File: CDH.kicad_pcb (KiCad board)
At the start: 2 copper layers, 45 parts, among them J3 G125-MH12605M4P, J4 Conn_ARM_JTAG_SWD_10, U1 STM32H745BITx, U2 MCP2562FDT-H_SN

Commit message: routing almost done
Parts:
- moved JP2 77.5 mm to (89.0, 37.0), turned to -90 degrees
- moved C27 73.1 mm to (77.0, 37.5)
- moved U2 72.1 mm to (81.8, 37.4)
- moved R6 69.8 mm to (88.5, 40.5), turned to -90 degrees
- moved C26 66.5 mm to (82.0, 41.0), turned to 0 degrees
- moved J4 62.8 mm to (29.0, 39.5), turned to 180 degrees
- moved PC104_H1 59.0 mm to (86.0, 55.0)
- moved J3 57.0 mm to (24.3, 55.4), turned to -90 degrees
- moved PC104_H2 52.2 mm to (90.0, 55.0)
- moved R8 51.4 mm to (40.8, 42.0), turned to 0 degrees
- moved C25 20.0 mm to (41.0, 76.0)
- moved SW_Reset1 17.6 mm to (41.0, 72.5)
- moved C24 14.5 mm to (34.5, 53.0)
- moved C28 10.8 mm to (82.9, 52.7), turned to 90 degrees
- moved R1 10.1 mm to (68.9, 37.7)
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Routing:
- net VDD: track 0.00 -> 74.9 mm
- net GND: track 0.00 -> 69.5 mm, vias 0 -> 2
- net /CS3: track 0.00 -> 52.7 mm
- net /CS2: track 0.00 -> 51.5 mm, vias 0 -> 1
- net Net-(JP1-B): track 0.00 -> 51.0 mm
- net /I2C2_SDA: track 0.00 -> 50.4 mm, vias 0 -> 1
- net /CS1: track 0.00 -> 50.3 mm
- net /I2C2_SCL: track 0.00 -> 49.7 mm, vias 0 -> 1
- net /FDCAN1_RX: track 0.00 -> 38.3 mm
- net /CANH_PC104: track 0.00 -> 29.2 mm
- net /CANL_PC104: track 0.00 -> 21.3 mm
- net /FDCAN1_TX: track 0.00 -> 15.1 mm
- net Net-(C23-Pad2): track 0.00 -> 13.8 mm
- net /CS5: track 0.00 -> 9.30 mm
- net VDDA: track 0.00 -> 7.16 mm
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- added copper zone on B.Cu, net GND
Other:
- board outline added: 72 x 50 mm
- board text added: "JTAG"
- board text added: "PAYLOAD"

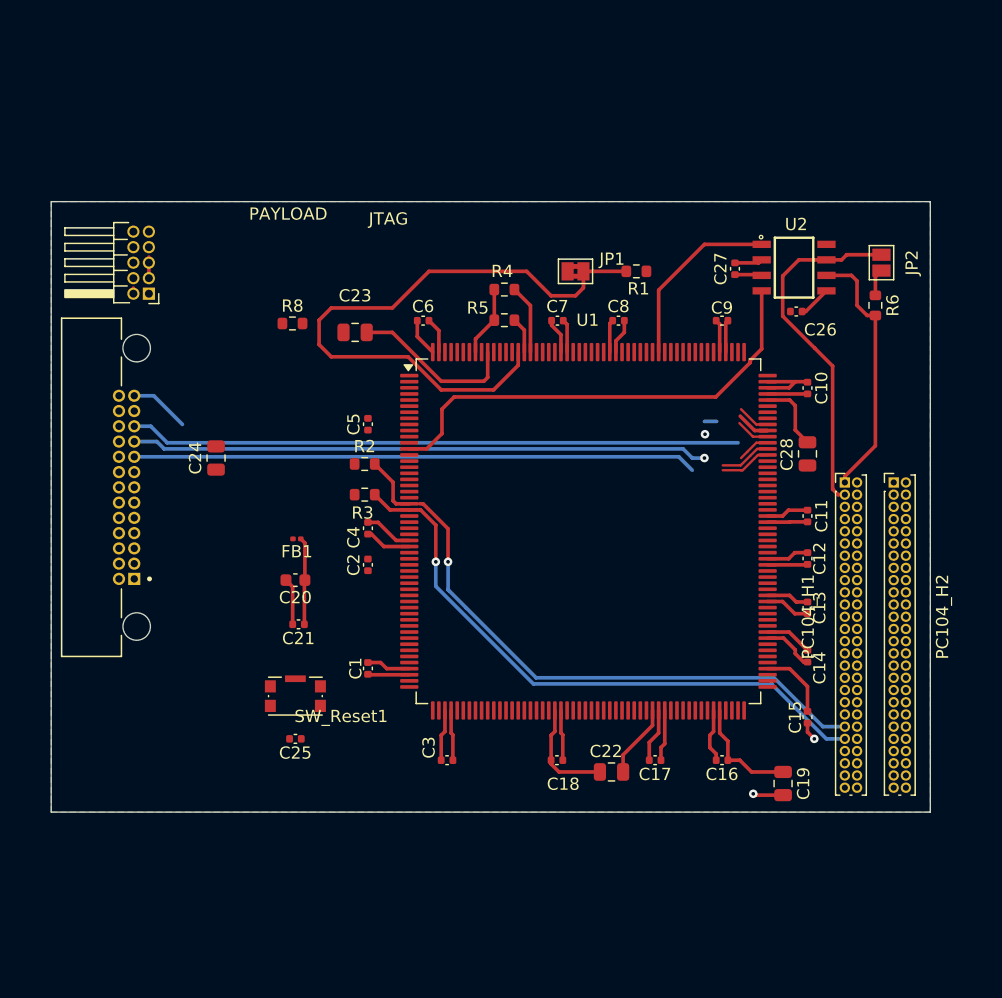
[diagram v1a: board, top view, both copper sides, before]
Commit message: changed STM32 symbol and made PCB 4 layers
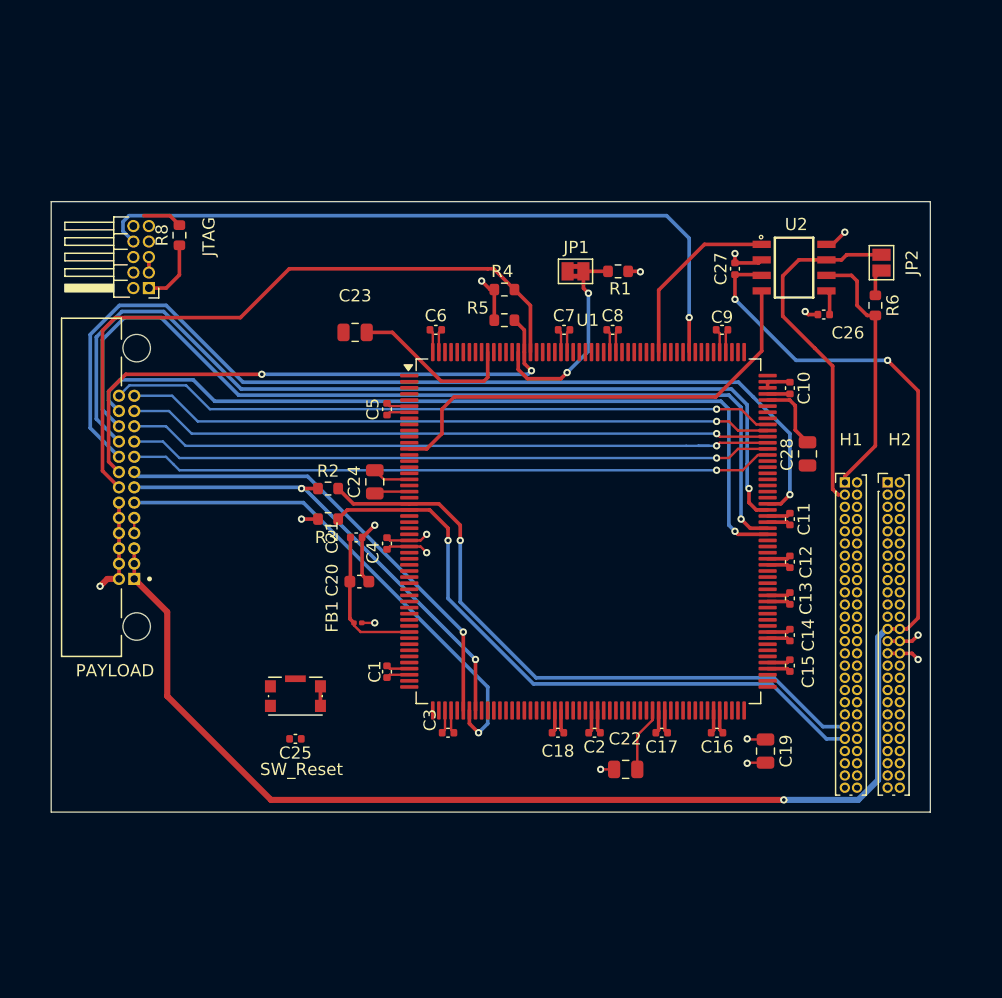
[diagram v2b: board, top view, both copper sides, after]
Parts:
- moved C2 23.1 mm to (65.5, 75.5), turned to 180 degrees
- moved C24 13.1 mm to (47.5, 55.0)
- moved R8 11.7 mm to (31.5, 34.8), turned to 90 degrees
- moved C21 8.55 mm to (46.0, 59.5), turned to 0 degrees
- moved FB1 8.50 mm to (46.1, 66.5), turned to 0 degrees
- moved C20 5.24 mm to (46.2, 63.1), turned to 0 degrees
- moved C15 4.47 mm to (81.5, 70.0), turned to 90 degrees
- moved R2 3.61 mm to (43.7, 55.5)
- moved R3 3.61 mm to (43.7, 58.0)
- moved C19 3.02 mm to (79.5, 77.0)
- moved C17 2.31 mm to (71.0, 75.5)
- moved C16 2.29 mm to (75.5, 75.5)
- moved C26 2.26 mm to (84.3, 41.2)
- moved C18 2.25 mm to (62.5, 75.5)
- moved C3 2.25 mm to (53.5, 75.5)
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- renumbered PC104_H1 to H1, PC104_H2 to H2, SW_Reset1 to SW_Reset
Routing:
- net +5V: track 2.21 -> 132.2 mm, vias 0 -> 3
- net /PAY4: track 0.00 -> 80.8 mm, vias 0 -> 1
- net /PAY3: track 0.00 -> 76.5 mm, vias 0 -> 1
- net /PAY2: track 0.00 -> 75.4 mm, vias 0 -> 1
- net /PAY1: track 0.00 -> 67.1 mm, vias 0 -> 1
- net /DEBUG_JTDI: track 0.00 -> 58.6 mm, vias 0 -> 1
- net /CS6: track 2.69 -> 54.8 mm, vias 0 -> 1
- net /I2C1_SCL: track 5.67 -> 55.6 mm
- net /CS4: track 2.98 -> 52.7 mm
- net /CS5: track 9.30 -> 53.7 mm, vias 0 -> 1
- net /I2C1_SDA: track 2.95 -> 47.0 mm, vias 0 -> 2
- net /SPI1_MISO: track 0.00 -> 41.4 mm, vias 0 -> 1
- net /SPI1_SCK: track 0.00 -> 38.8 mm, vias 0 -> 1
- net /SPI1_MOSI: track 0.00 -> 38.0 mm, vias 0 -> 1
- net Net-(JP1-B): track 51.0 -> 17.1 mm, vias 0 -> 2
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- added copper zone on In1.Cu, net GND
- added copper zone on In2.Cu, net VDD
- removed copper zone on B.Cu, net GND
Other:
- copper layers 2 -> 4
